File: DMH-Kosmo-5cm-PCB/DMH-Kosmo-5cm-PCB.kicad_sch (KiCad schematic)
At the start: 0 parts

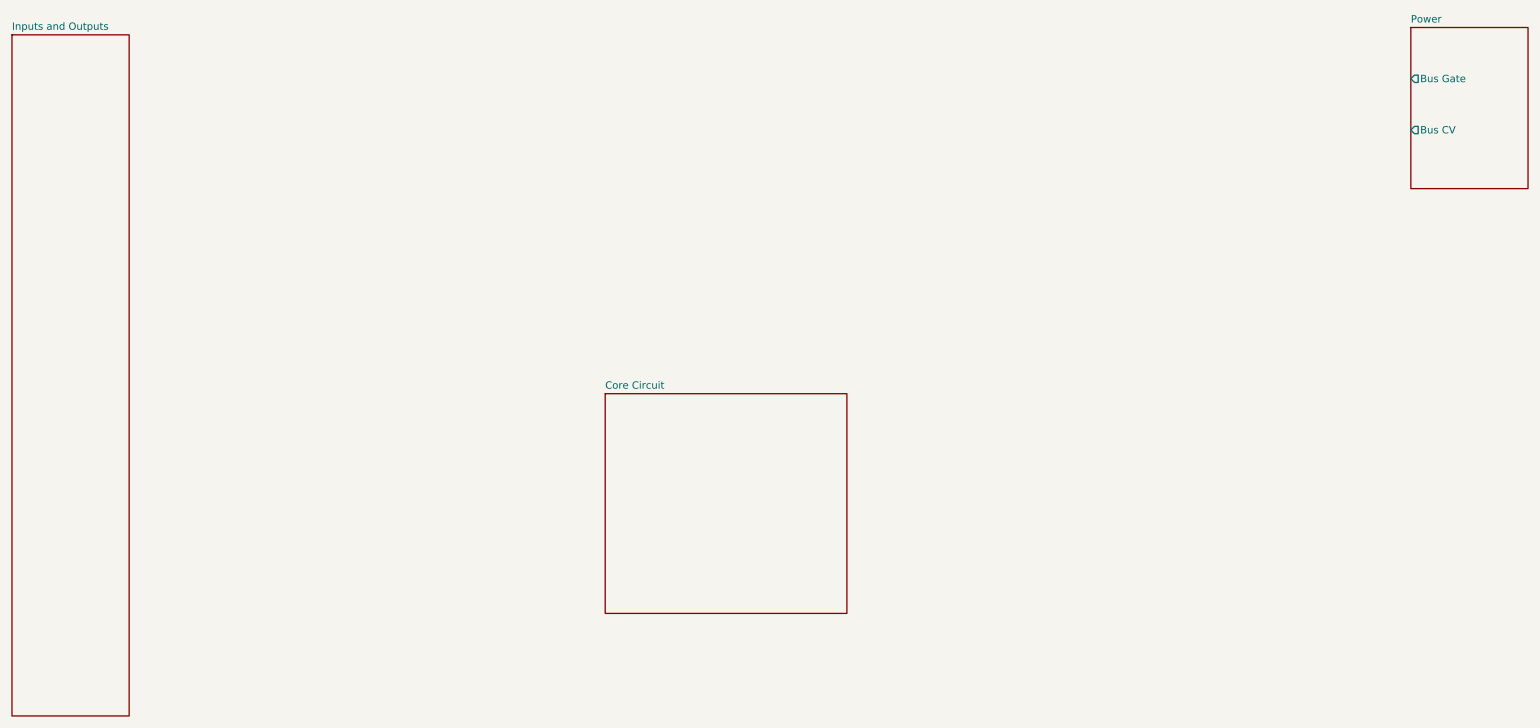
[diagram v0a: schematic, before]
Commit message: Minor fixes on schematic templates
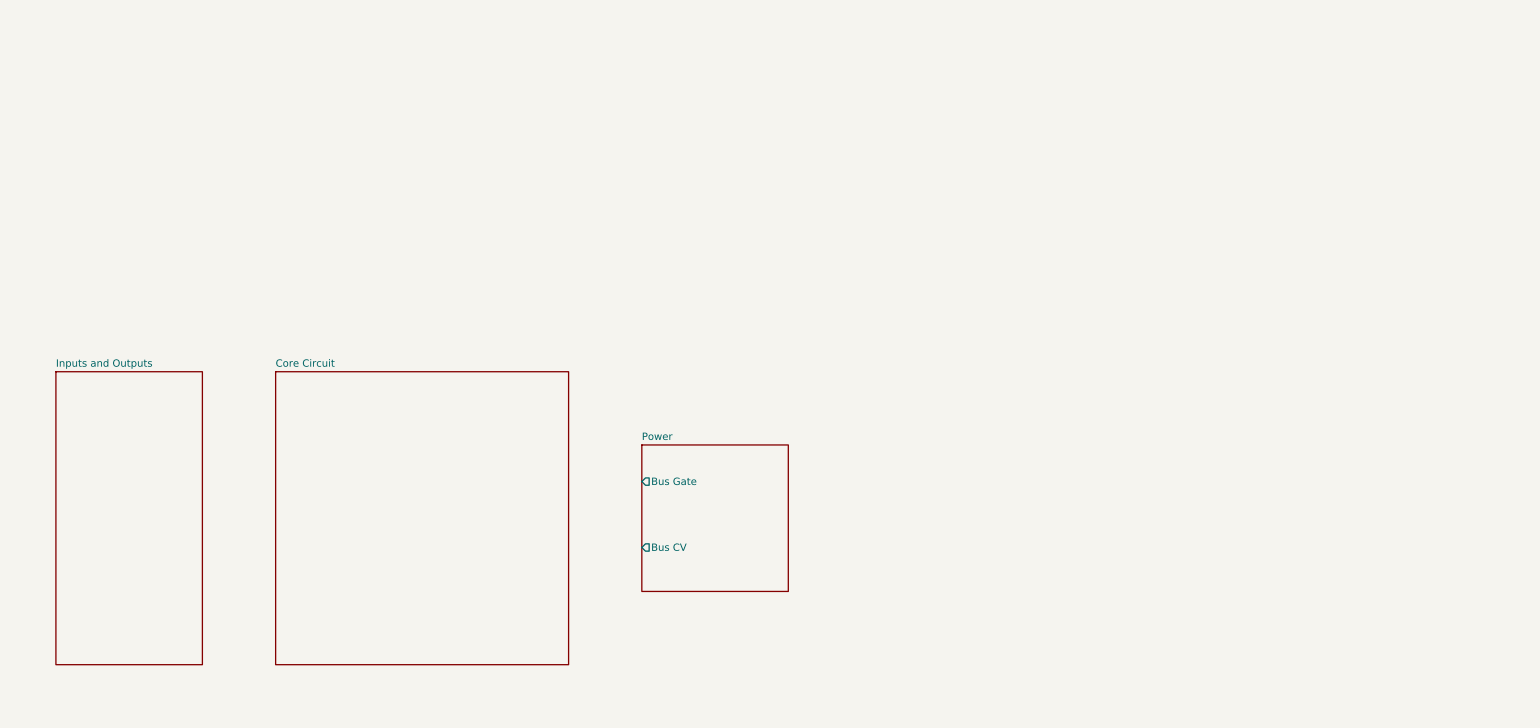
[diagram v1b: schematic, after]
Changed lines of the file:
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@@
 	)
 	(sheet
-		(at 260.35 16.51)
-		(size 20.32 27.94)
+		(at 127 88.9)
+		(size 25.4 25.4)
 		(fields_autoplaced yes)
 		(stroke
@@
 		)
 		(property "Sheetname" "Power"
-			(at 260.35 15.7984 0)
+			(at 127 88.1884 0)
 			(effects
 				(font
@@
 		)
 		(property "Sheetfile" "Power.kicad_sch"
-			(at 260.35 45.0346 0)
+			(at 127 114.8846 0)
 			(effects
 				(font
@@
 		)
 		(pin "Bus Gate" output
-			(at 260.35 25.4 180)
+			(at 127 95.25 180)
 			(effects
 				(font
@@
 		)
 		(pin "Bus CV" output
-			(at 260.35 34.29 180)
+			(at 127 106.68 180)
 			(effects
 				(font
@@
 	)
 	(sheet
-		(at 120.65 80.01)
-		(size 41.91 38.1)
+		(at 63.5 76.2)
+		(size 50.8 50.8)
 		(fields_autoplaced yes)
 		(stroke
@@
 		)
 		(property "Sheetname" "Core Circuit"
-			(at 120.65 79.2984 0)
+			(at 63.5 75.4884 0)
 			(effects
 				(font
@@
 		)
 		(property "Sheetfile" "Core_Circuit.kicad_sch"
-			(at 120.65 118.6946 0)
+			(at 63.5 127.5846 0)
 			(effects
 				(font
@@
 	)
 	(sheet
-		(at 17.78 17.78)
-		(size 20.32 118.11)
+		(at 25.4 76.2)
+		(size 25.4 50.8)
 		(fields_autoplaced yes)
 		(stroke
@@
 		)
 		(property "Sheetname" "Inputs and Outputs"
-			(at 17.78 17.0684 0)
+			(at 25.4 75.4884 0)
 			(effects
 				(font
@@
 		)
 		(property "Sheetfile" "Inputs_and_Outputs.kicad_sch"
-			(at 17.78 136.4746 0)
+			(at 25.4 127.5846 0)
 			(effects
 				(font
